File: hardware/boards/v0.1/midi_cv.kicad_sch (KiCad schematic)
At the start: 16 parts, among them J10 MIDI_OUT/THRU, J11 MIDI_IN, U19 TLP2362TPR_E

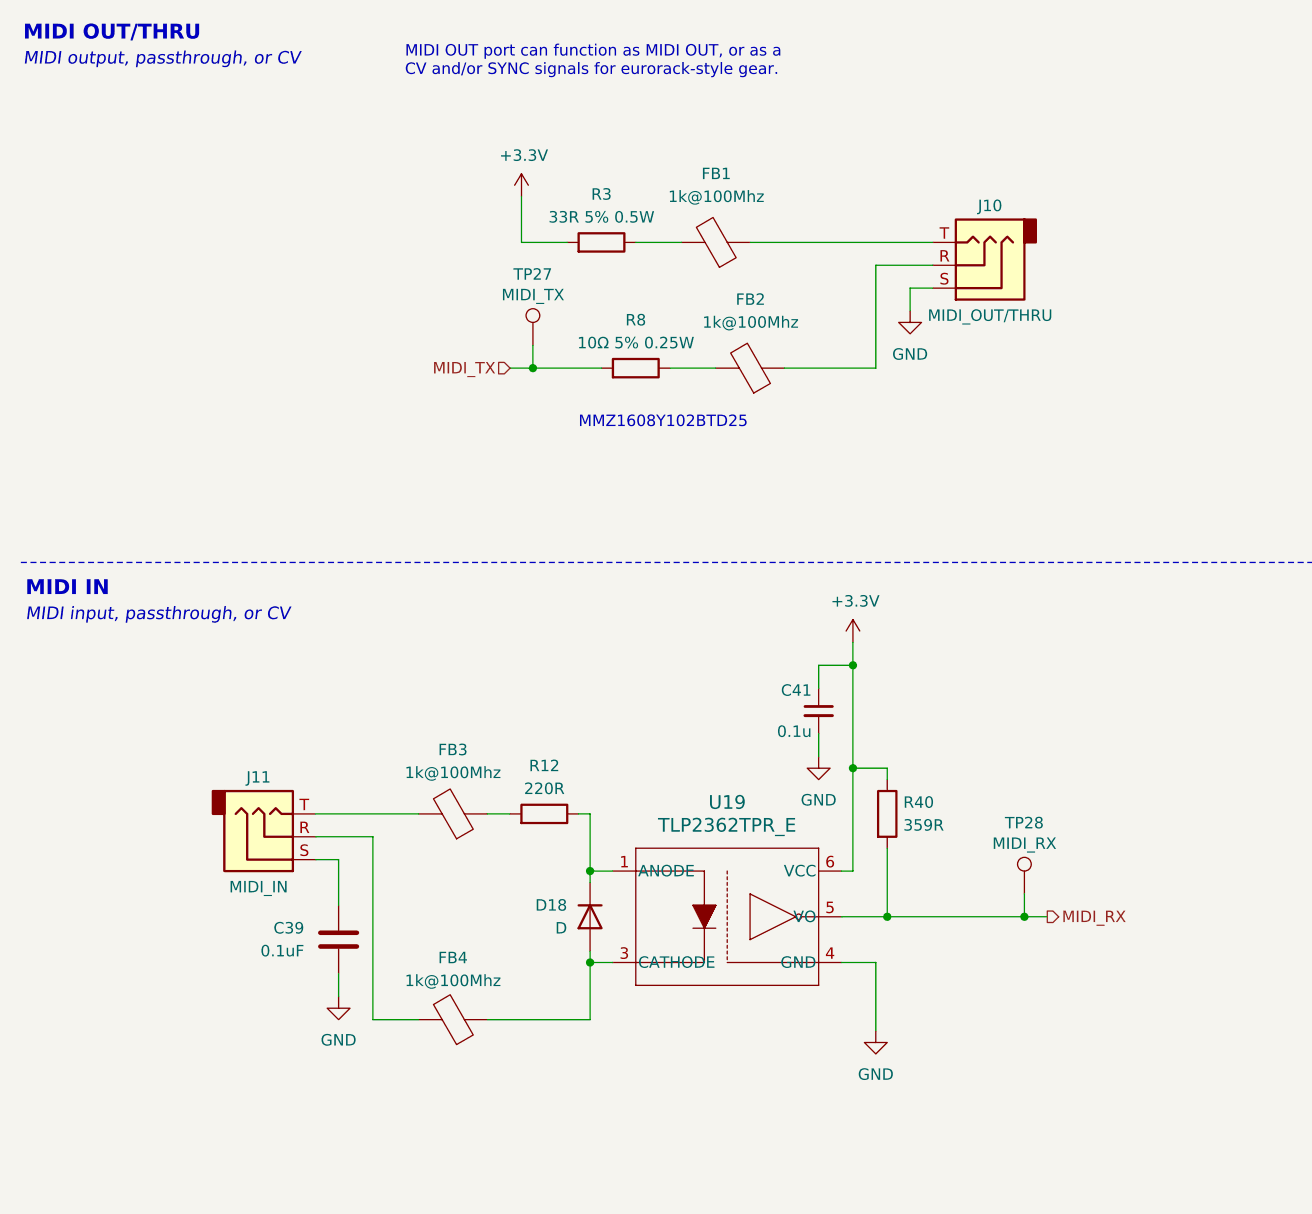
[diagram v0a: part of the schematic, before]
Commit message: feat: routing cleanup and start of BOM selection
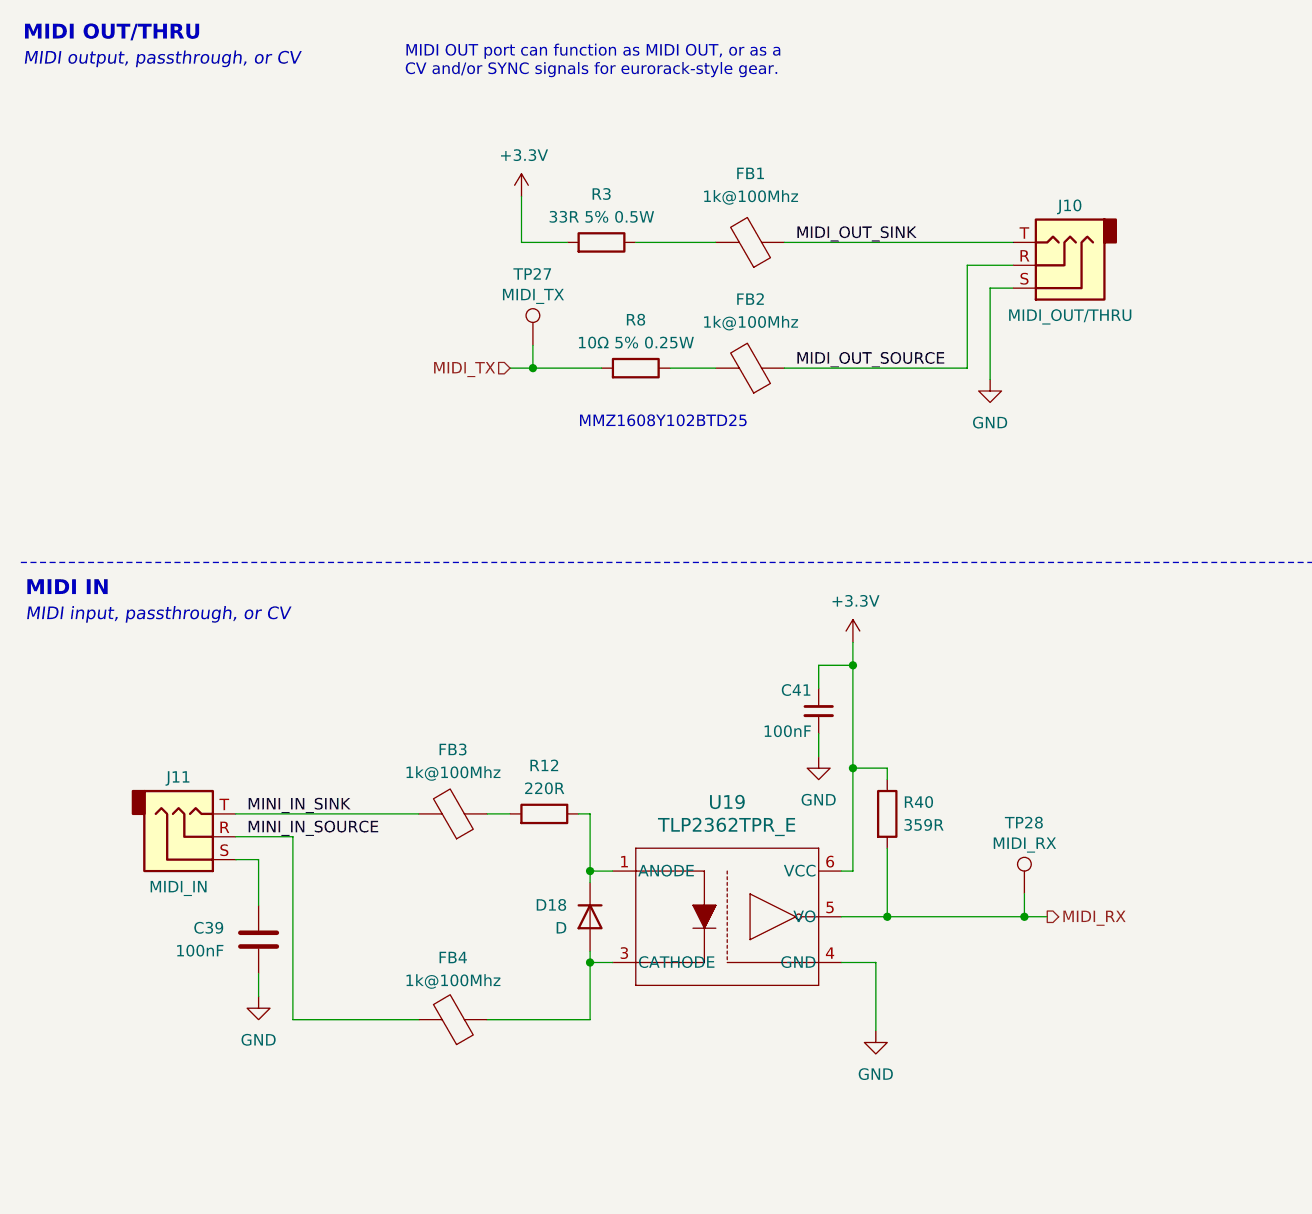
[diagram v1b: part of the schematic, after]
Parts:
- C39: value 0.1uF -> 100nF; footprint Capacitor_SMD:C_0603_1608Metric -> Capacitor_SMD:C_0402_1005Metric; JLC (none) -> C1525
- C41: value 0.1u -> 100nF; footprint Capacitor_SMD:C_0603_1608Metric -> Capacitor_SMD:C_0402_1005Metric; JLC (none) -> C1525
- FB1, FB2, FB3, FB4: JLC (none) -> C50069
- J10, J11: JLC C4991872 -> (none)
- TP27, TP28: now left out of the parts list
- U19: JLC (none) -> C5156050
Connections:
- net MINI_IN_SINK: now reaches FB3.2, J11.T
- net MINI_IN_SOURCE: now reaches FB4.2, J11.R
- net MIDI_OUT_SOURCE: now reaches FB2.1, J10.R
- net MIDI_OUT_SINK: now reaches FB1.1, J10.T
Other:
- moved on the sheet: C39, FB1, J10, J11

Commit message: feat: update various components to 0402
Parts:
- R12, R3, R40, R8: footprint Resistor_SMD:R_0603_1608Metric -> Resistor_SMD:R_0402_1005Metric

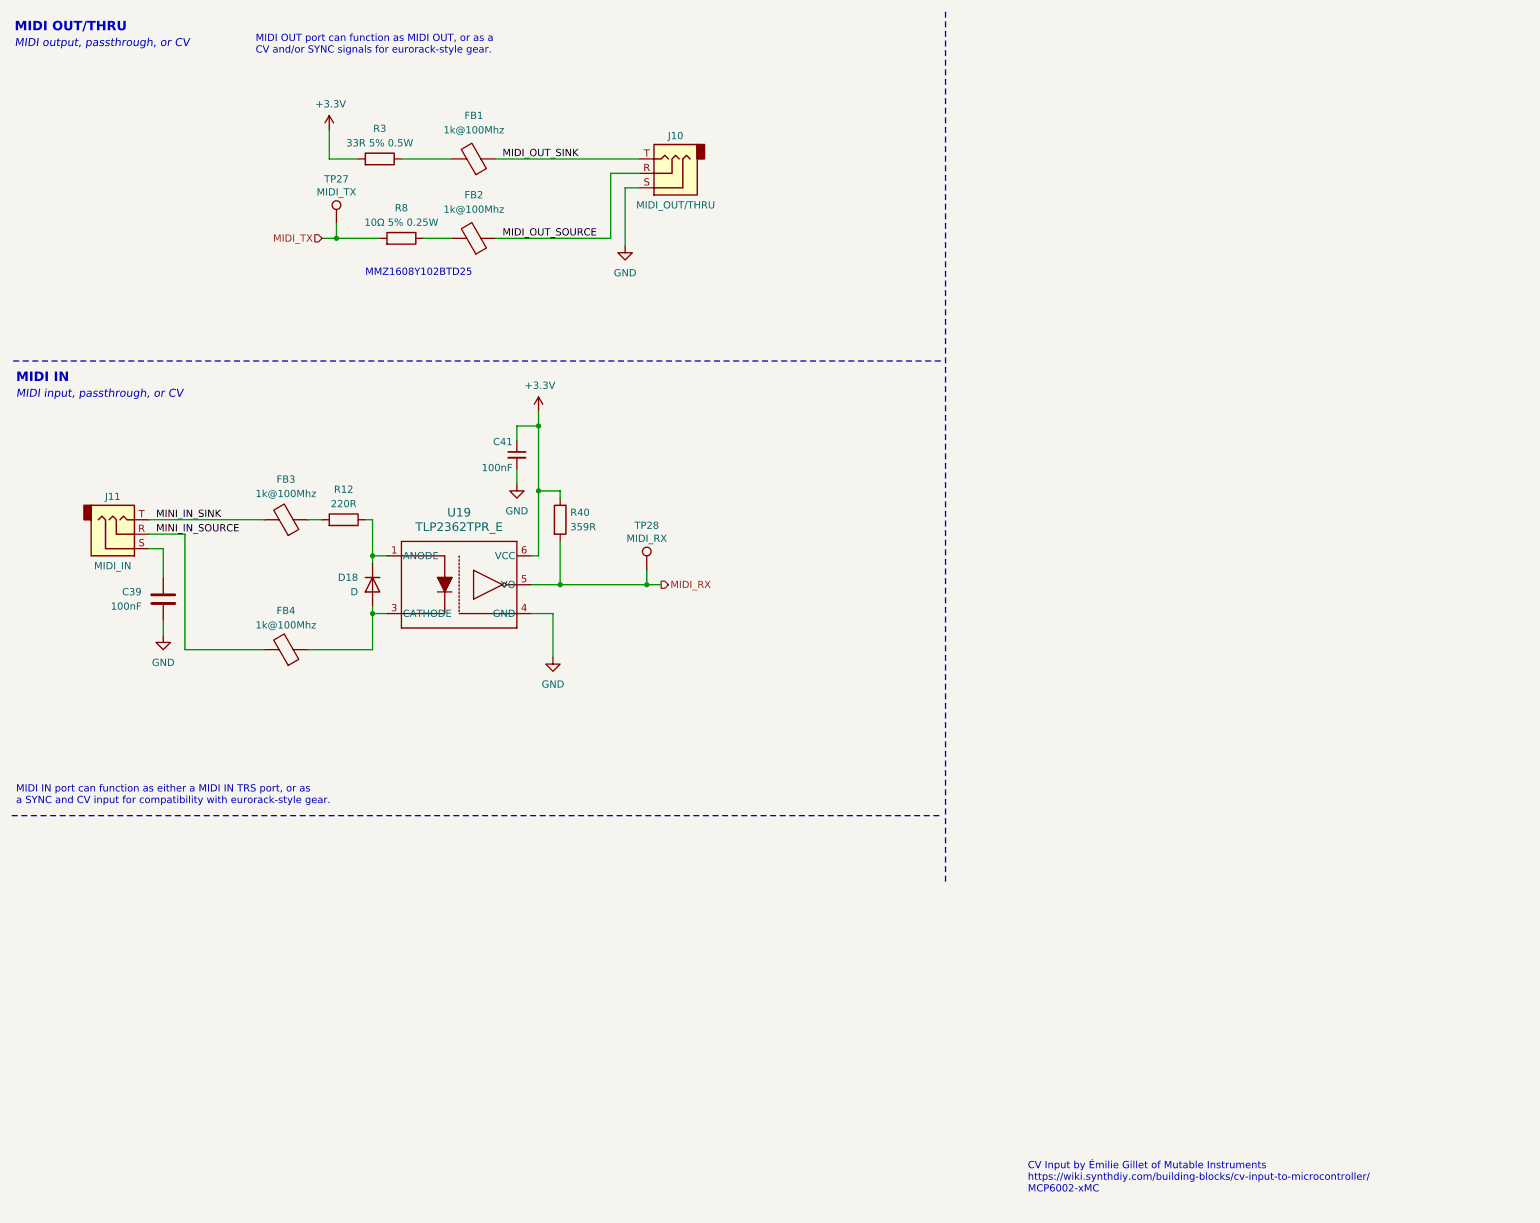
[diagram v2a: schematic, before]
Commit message: feat: various routing cleanup, add SD flash
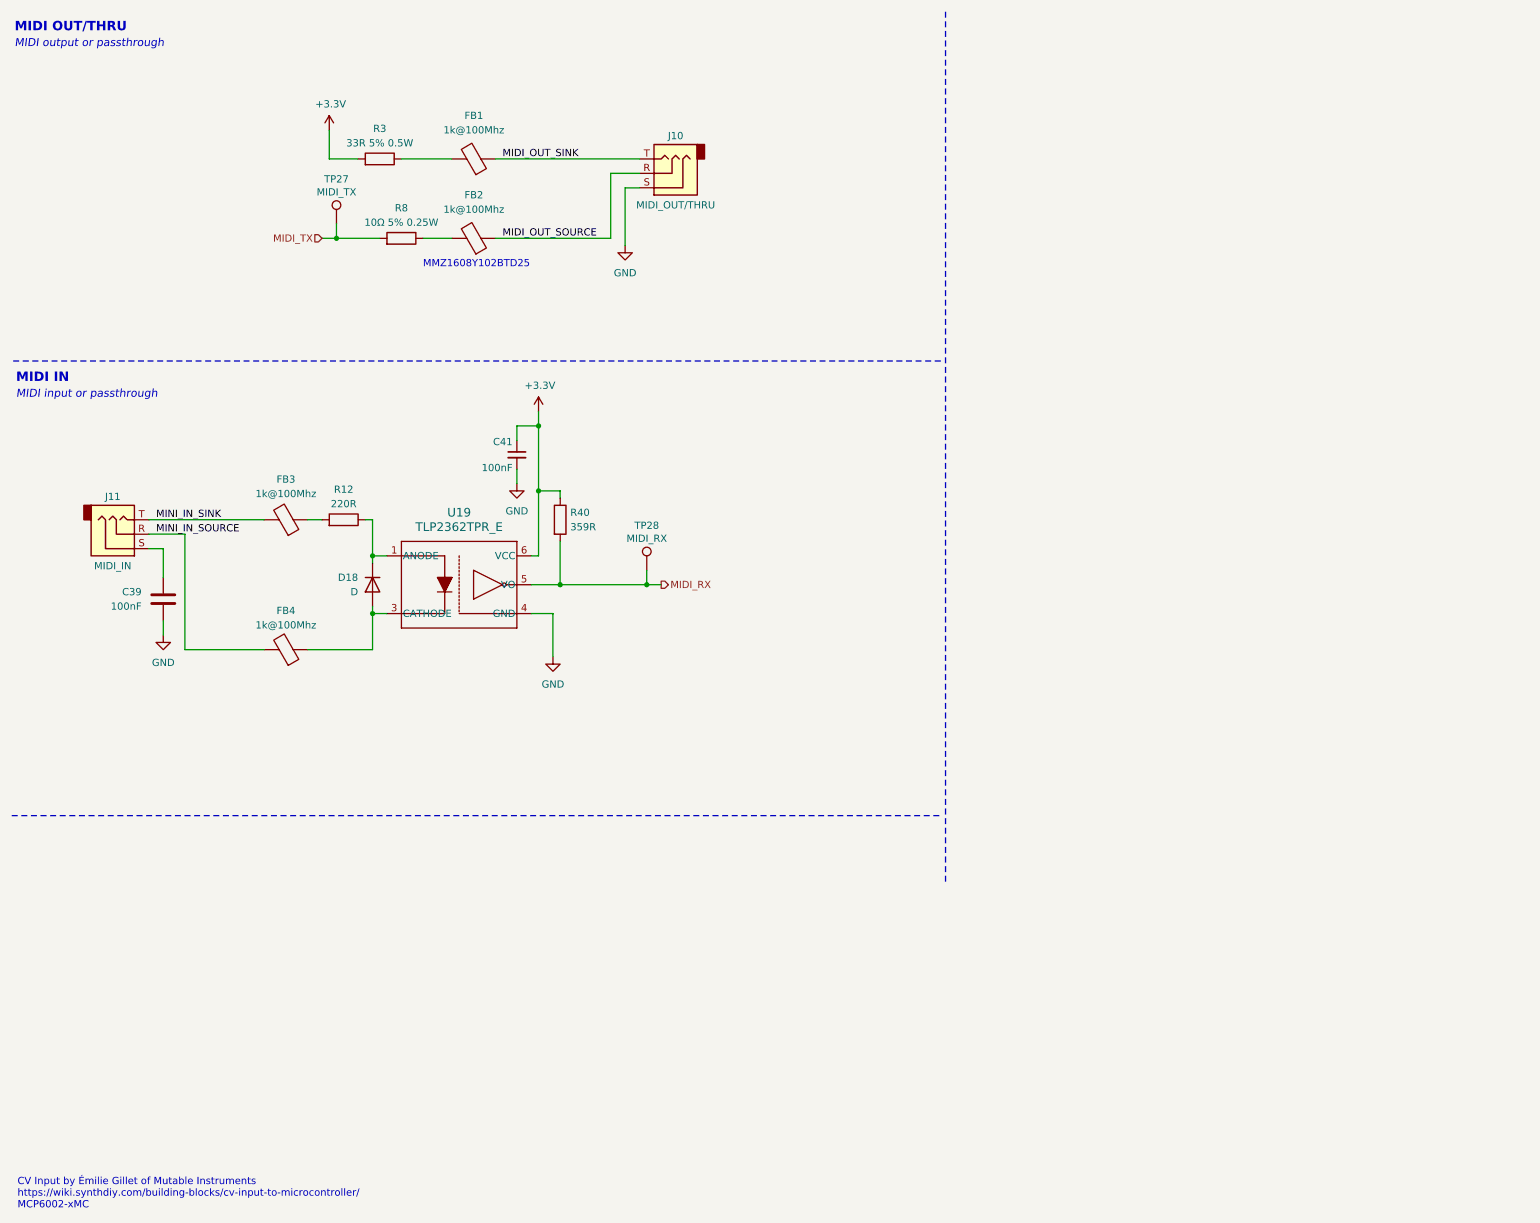
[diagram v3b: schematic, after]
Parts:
- FB1, FB2, FB3, FB4: JLC C50069 -> C531293
- J10, J11: now left out of the parts list
- R12: JLC (none) -> C25091
- R3: footprint Resistor_SMD:R_0402_1005Metric -> Resistor_SMD:R_1206_3216Metric; JLC (none) -> C414914
- R8: JLC (none) -> C427198
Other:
- note added: "MIDI input or passthrough"
- note added: "MIDI output or passthrough"
- note removed: "MIDI IN port can function as either a MIDI IN TRS port, or as a SYNC and CV input for compatibility with eurorack-style gear."
- note removed: "MIDI OUT port can function as MIDI OUT, or as a CV and/or SYNC signals for eurorack-style gear."
- note removed: "MIDI input, passthrough, or CV"
- note removed: "MIDI output, passthrough, or CV"

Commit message: feat: more BOM selection
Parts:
- D18: value D -> 1N4148WS; footprint Diode_SMD:D_0603_1608Metric -> Diode_SMD:D_SOD-323; JLC (none) -> C2128
- R40: value 359R -> 1.8k; footprint Resistor_SMD:R_0402_1005Metric -> Resistor_SMD:R_0603_1608Metric; JLC (none) -> C4177
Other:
- note added: "(CA-033) MIDI 1.0 Electrical Specification Update [2014] https://midi.org/5-pin-din-electrical-specs rp54 Specification for Use of TRS Connectors with MIDI Devices https://midi.org/specification-for-use-of-trs-connectors-with-midi-devices"
- note added: "https://midi.org/community/midi-hardware/best-optoisolator-for-3-3v https://www.reddit.com/r/AskElectronics/comments/9ommpm/choosing_the_right_optocoupler_for_use_with_midi/ "3.3 V SMD variants of the 6N137: ACPL-M60L, ACPL-M62L, FODM8061, PS9124, TLP2362""

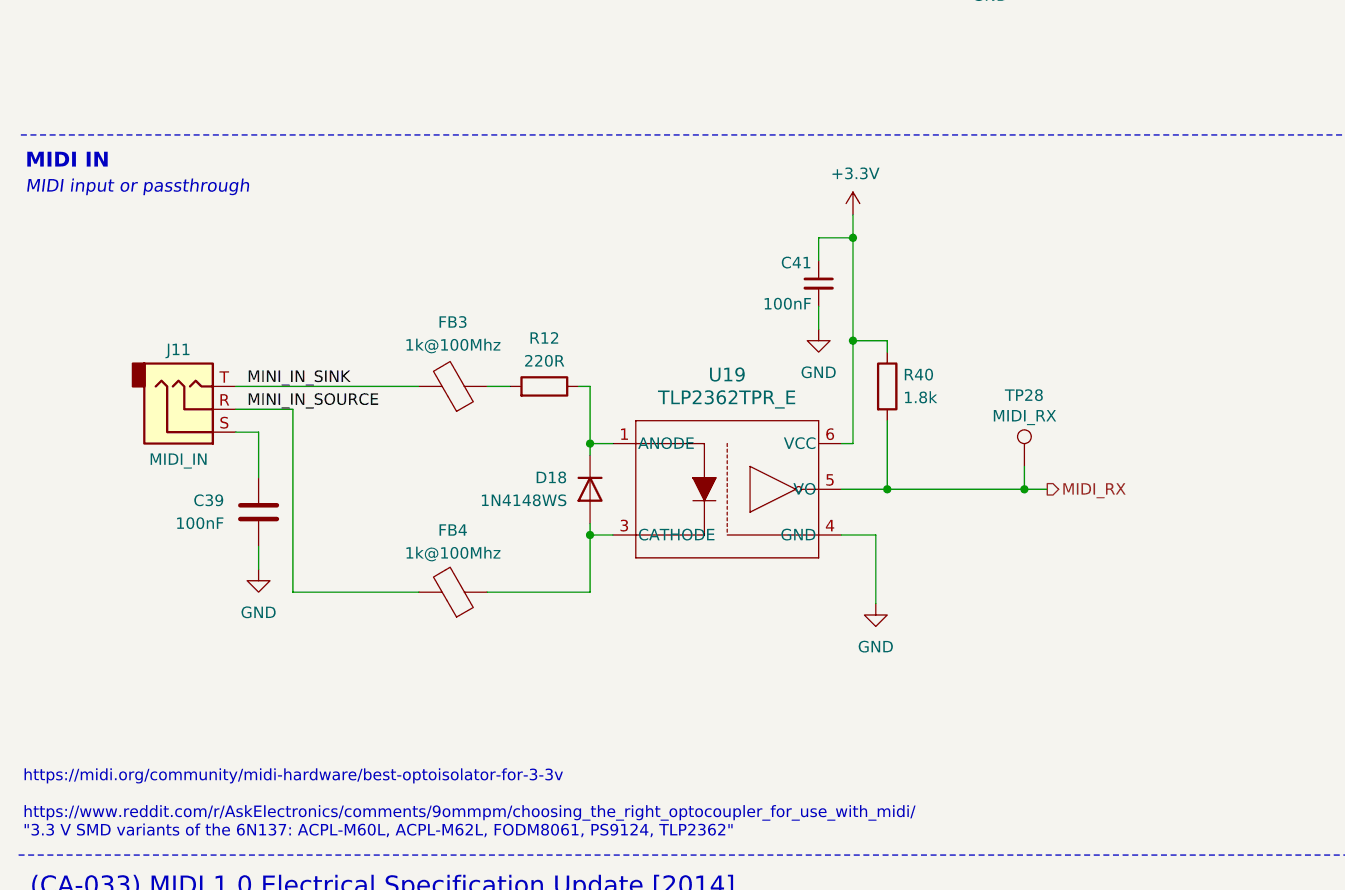
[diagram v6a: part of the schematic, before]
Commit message: feat: various layout and routing adjustments
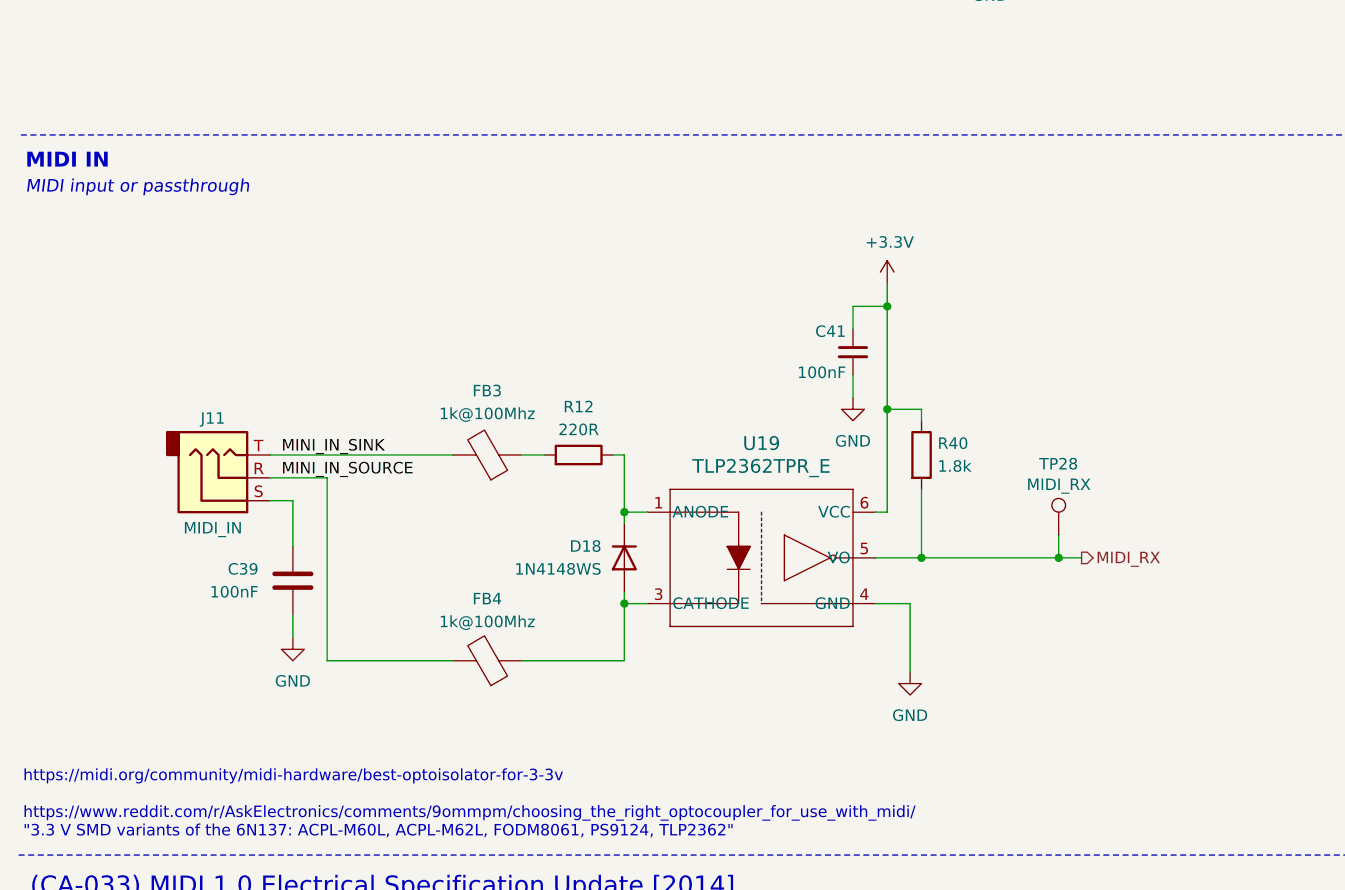
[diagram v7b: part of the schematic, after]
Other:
- moved on the sheet: C39, C41, D18, FB3, FB4, J11, R12, R40, TP28, U19
